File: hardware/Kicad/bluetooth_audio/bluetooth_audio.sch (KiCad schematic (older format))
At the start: 23 parts

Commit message: Kicad project started
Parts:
- removed J?: AVR-ISP-6, symbol Connector:AVR-ISP-6
- removed J?: Conn_01x03, symbol Connector_Generic:Conn_01x03
- removed M?: CSR8645, symbol Project_lib:CSR8645
- removed M?: TPA6112_M, symbol Project_lib:TPA6112_M
- removed R? (x2): 200, symbol Device:R
- removed R? (x8): 10K, symbol Device:R
- removed R? (x8): 20K, symbol Device:R
- removed U?: ATmega8-16AU, Package_QFP:TQFP-32_7x7mm_P0.8mm, symbol MCU_Microchip_ATmega:ATmega8-16AU
- added M?: CSR8645, symbol modules:CSR8645
- added U1: ATmega8A-AU, Package_QFP:TQFP-32_7x7mm_P0.8mm, symbol MCU_Microchip_ATmega:ATmega8A-AU
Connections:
- net labels added: VDD
- net labels removed: +3V3, +5V, BR_RST, BT_RST, BT_RX, BT_TX, MUTE, NXT, PP, PRV, PWR, V+, V-
- wire segments 99 -> 10
- no-connect marks 29 -> 26

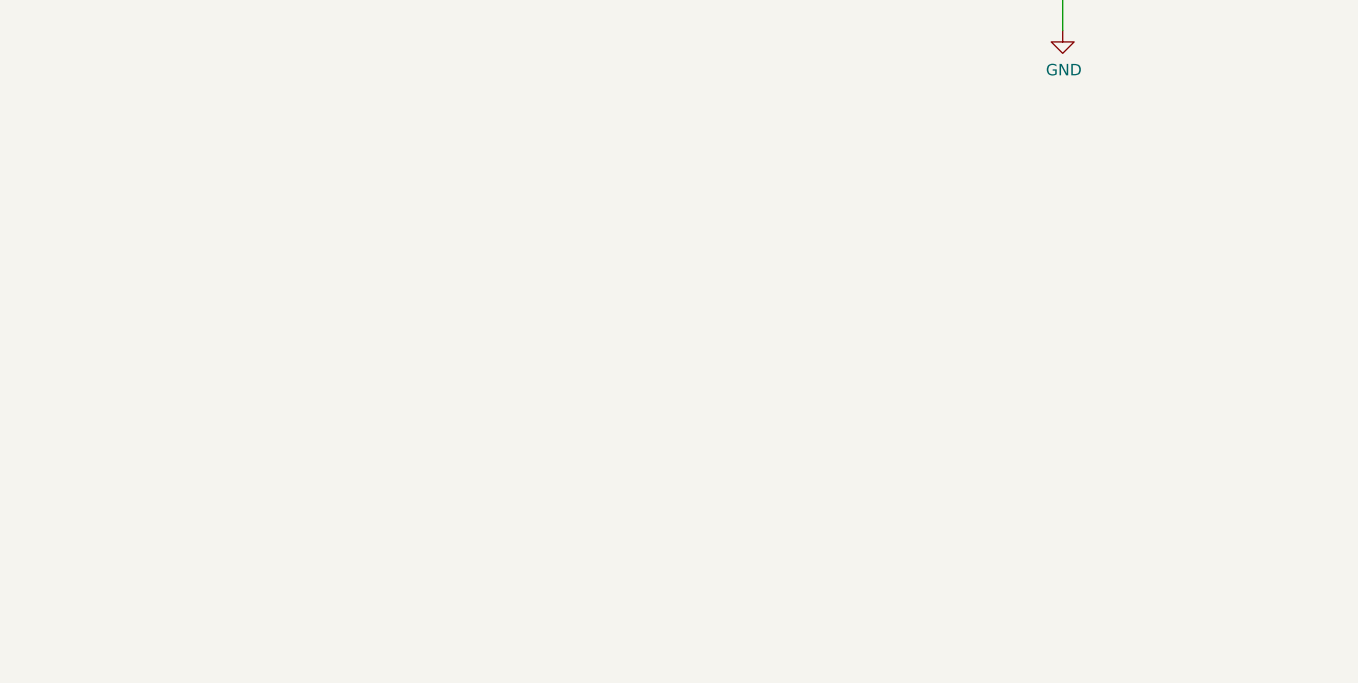
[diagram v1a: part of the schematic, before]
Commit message: Расчитал DC-DC
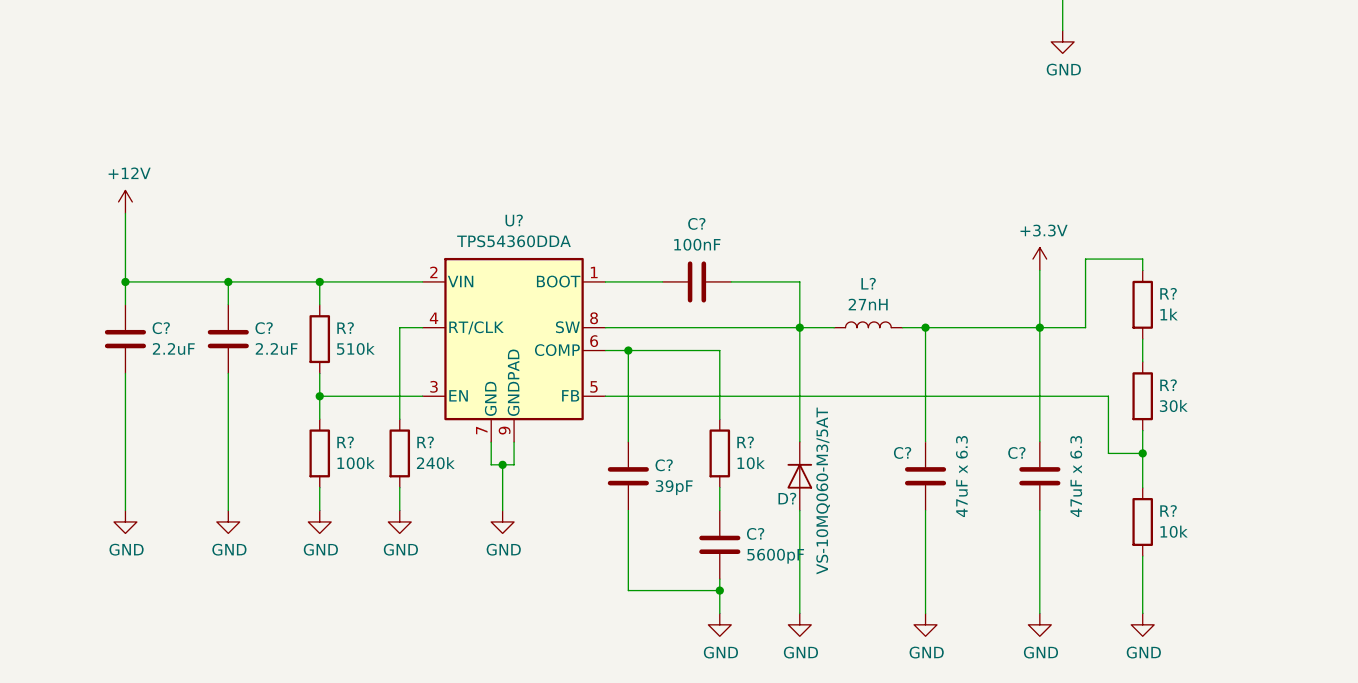
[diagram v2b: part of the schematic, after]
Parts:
- added C?: 100nF, Capacitor_SMD:C_0805_2012Metric, symbol Device:C
- added C?: 39pF, Capacitor_SMD:C_0805_2012Metric, symbol Device:C
- added C?: 5600pF, Capacitor_SMD:C_0805_2012Metric, symbol Device:C
- added C? (x2): 47uF x 6.3, Capacitor_SMD:C_1206_3216Metric_Pad1.42x1.75mm_HandSolder, symbol Device:C
- added C? (x2): 2.2uF, Capacitor_SMD:C_1812_4532Metric_Pad1.30x3.40mm_HandSolder, symbol Device:C
- added D?: VS-10MQ060-M3/5AT, Diode_SMD:D_SMA, symbol Device:D
- added L?: 27nH, Inductor_SMD:L_0805_2012Metric_Pad1.15x1.40mm_HandSolder, symbol Device:L
- added R?: 510k, Resistor_SMD:R_0805_2012Metric_Pad1.15x1.40mm_HandSolder, symbol Device:R
- added R?: 100k, Resistor_SMD:R_0805_2012Metric_Pad1.15x1.40mm_HandSolder, symbol Device:R
- added R?: 240k, Resistor_SMD:R_0805_2012Metric_Pad1.15x1.40mm_HandSolder, symbol Device:R
- added R? (x2): 10k, Resistor_SMD:R_0805_2012Metric_Pad1.15x1.40mm_HandSolder, symbol Device:R
- added R?: 30k, Resistor_SMD:R_0805_2012Metric_Pad1.15x1.40mm_HandSolder, symbol Device:R
- added R?: 1k, Resistor_SMD:R_0805_2012Metric_Pad1.15x1.40mm_HandSolder, symbol Device:R
- added U?: TPS54360DDA, Package_SO:TI_SO-PowerPAD-8_ThermalVias, symbol Regulator_Switching:TPS54360DDA
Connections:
- net GND: now also C?.1, C?.1, C?.2, C?.2, C?.2, C?.2, D?.2 (A), R?.2, R?.2, R?.2, U?.7 (GND), U?.9 (GNDPAD)
- new net: C?.2, U?.1 (BOOT)
- new net: R?.1, R?.2, U?.3 (EN)
- new net: R?.1, U?.4 (RT/CLK)
- new net: R?.1, R?.2, U?.5 (FB)
- new net: C?.1, R?.1, U?.6 (COMP)
- new net: C?.1, D?.1 (K), L?.1, U?.8 (SW)
- new net: C?.1, R?.2
- new net: R?.1, R?.2
- new net +12V: C?.1, C?.1, R?.1, U?.2 (VIN)
- new net +3V3: C?.2, C?.2, L?.2, R?.1
